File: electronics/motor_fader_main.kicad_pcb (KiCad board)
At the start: 2 copper layers, 59 x 17 mm, 30 parts, among them J1 Conn_01x04_MountingPin, J2 Program, J3 Conn_01x04_MountingPin, U1 ATtiny1616-M, U2 DRV8837

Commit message: Board cleanup, BOM cleanup
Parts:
- moved D2 0.75 mm to (75.2, 57.5)
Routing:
- net GND: track 8.58 -> 17.3 mm
- net VCC: track 95.3 -> 93.2 mm

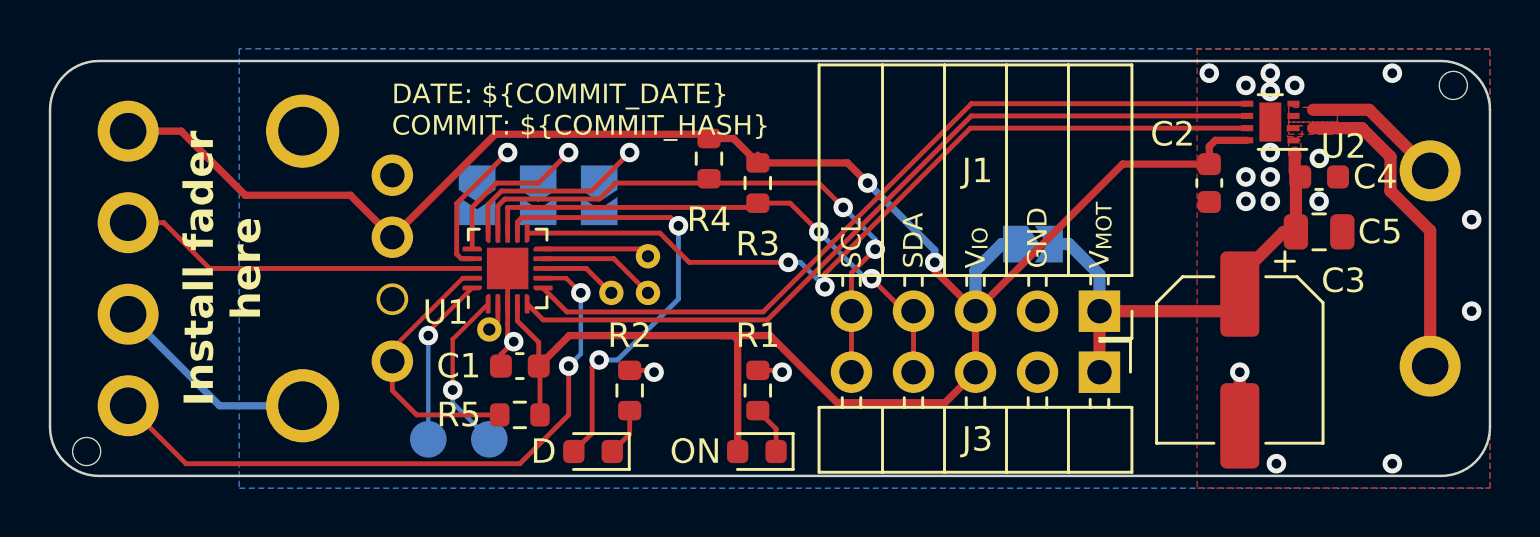
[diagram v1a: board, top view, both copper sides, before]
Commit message: Add JST SH I2C connectors
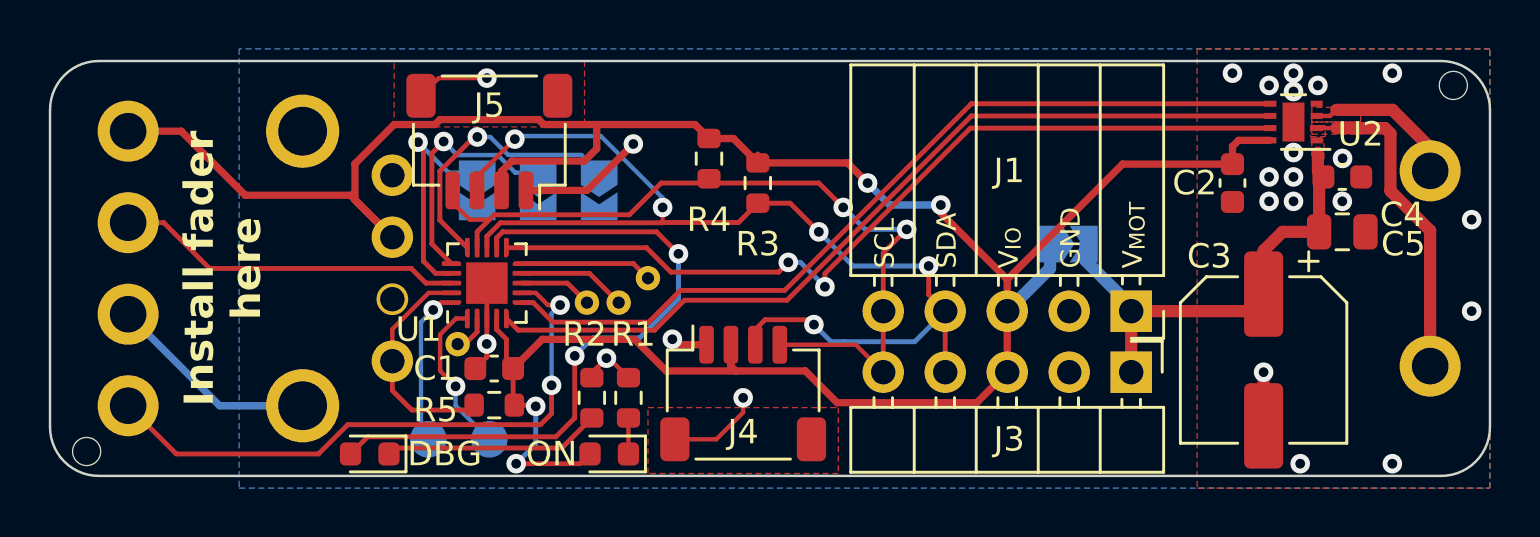
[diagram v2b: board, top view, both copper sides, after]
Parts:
- added J4: Conn_01x04_MountingPin, Connector_JST:JST_SH_SM04B-SRSS-TB_1x04-1MP_P1.00mm_Horizontal, F.Cu at (81.4, 55.1)
- added J5: Conn_01x04_MountingPin, Connector_JST:JST_SH_SM04B-SRSS-TB_1x04-1MP_P1.00mm_Horizontal, F.Cu at (71.0, 44.8)
- J1, J3: value Conn_01x04_MountingPin -> Conn_01x05
- moved D2 9.15 mm to (66.1, 57.6)
- moved D1 6.05 mm to (75.9, 57.6)
- moved R1 5.31 mm to (76.7, 55.3)
- moved R2 1.58 mm to (75.2, 55.3)
- moved TP6 1.43 mm to (69.7, 53.1)
- moved JP4 1.42 mm to (94.7, 49.0)
- moved J1 1.30 mm to (97.3, 51.8)
- moved J3 1.30 mm to (97.3, 54.2)
- moved TP5 1.26 mm to (76.3, 51.4)
- moved R5 1.12 mm to (71.2, 55.6)
- moved TP1 1.08 mm to (75.0, 51.4)
- moved C1 1.05 mm to (71.2, 54.1)
- moved U1 1.04 mm to (70.9, 50.6)
- moved C3 0.97 mm to (102.7, 53.8)
- moved C2 0.95 mm to (101.5, 46.5)
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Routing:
- net /SDA: track 22.1 -> 45.2 mm, vias 2 -> 5
- net VCC: track 93.2 -> 108.0 mm, vias 2 -> 4
- net GND: track 17.3 -> 30.4 mm, vias 21 -> 24
- net /SCL: track 23.8 -> 33.1 mm
- net /DBG_LED: track 18.7 -> 27.7 mm
- net Net-(D2-K): track 1.97 -> 8.92 mm
- net /M_1: track 33.2 -> 35.1 mm
- net /M_2: track 32.8 -> 34.7 mm
- net /M_SLEEP: track 33.4 -> 35.3 mm
- net /A0: track 7.42 -> 9.26 mm
- net /A2: track 9.53 -> 11.3 mm
- net /UPDI: track 11.0 -> 9.32 mm
- net /A1: track 8.26 -> 9.93 mm
- net /R_FADER: track 26.9 -> 25.2 mm
- net /MOTOR_B: track 12.9 -> 14.2 mm
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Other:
- board text added: "DBG"
- board text removed: "D"

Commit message: 3d model and update links in readme
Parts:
- J4, J5: footprint Connector_JST:JST_SH_SM04B-SRSS-TB_1x04-1MP_P1.00mm_Horizontal -> modified:JST_SH_SM04B-SRSS-TB_1x04-1MP_P1.00mm_Horizontal
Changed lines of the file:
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@@
 		)
 	)
-	(footprint "Connector_JST:JST_SH_SM04B-SRSS-TB_1x04-1MP_P1.00mm_Horizontal"
+	(footprint "modified:JST_SH_SM04B-SRSS-TB_1x04-1MP_P1.00mm_Horizontal"
 		(layer "F.Cu")
 		(at 81.4 55.125)
@@
 			)
 		)
-		(property "Footprint" "Connector_JST:JST_SH_SM04B-SRSS-TB_1x04-1MP_P1.00mm_Horizontal"
+		(property "Footprint" "modified:JST_SH_SM04B-SRSS-TB_1x04-1MP_P1.00mm_Horizontal"
 			(at 0 0 0)
 			(unlocked yes)
@@
 		)
 		(model "${KICAD8_3DMODEL_DIR}/Connector_JST.3dshapes/JST_SH_SM04B-SRSS-TB_1x04-1MP_P1.00mm_Horizontal.wrl"
+			(hide yes)
 			(offset
 				(xyz 0 0 0)
@@
 			(rotate
 				(xyz 0 0 0)
+			)
+		)
+		(model "${KIPRJMOD}/lib/misc.3dmodels/SM04B-SRSS-TB.STEP"
+			(offset
+				(xyz 0 1.3 -0.3)
+			)
+			(scale
+				(xyz 1 1 1)
+			)
+			(rotate
+				(xyz -90 0 0)
 			)
 		)
@@
 		)
 	)
-	(footprint "Connector_JST:JST_SH_SM04B-SRSS-TB_1x04-1MP_P1.00mm_Horizontal"
+	(footprint "modified:JST_SH_SM04B-SRSS-TB_1x04-1MP_P1.00mm_Horizontal"
 		(layer "F.Cu")
 		(at 71 44.8 180)
@@
 		(tags "connector JST SH horizontal")
 		(property "Reference" "J5"
-			(at 0 1.475 0)
+			(at 0 1.575 180)
 			(layer "F.SilkS")
 			(effects
@@
 		)
 		(property "Value" "Conn_01x04_MountingPin"
-			(at 0 3.98 0)
-			(layer "F.Fab")
-			(effects
-				(font
-					(size 1 1)
-					(thickness 0.15)
-				)
-			)
-		)
-		(property "Footprint" "Connector_JST:JST_SH_SM04B-SRSS-TB_1x04-1MP_P1.00mm_Horizontal"
+			(at 0 3.98 180)
+			(layer "F.Fab")
+			(effects
+				(font
+					(size 1 1)
+					(thickness 0.15)
+				)
+			)
+		)
+		(property "Footprint" "modified:JST_SH_SM04B-SRSS-TB_1x04-1MP_P1.00mm_Horizontal"
 			(at 0 0 180)
 			(unlocked yes)
@@
 		)
 		(fp_text user "${REFERENCE}"
-			(at 0 0 0)
+			(at 0 0 180)
 			(layer "F.Fab")
 			(effects
@@
 		)
 		(model "${KICAD8_3DMODEL_DIR}/Connector_JST.3dshapes/JST_SH_SM04B-SRSS-TB_1x04-1MP_P1.00mm_Horizontal.wrl"
+			(hide yes)
 			(offset
 				(xyz 0 0 0)
@@
 			)
 		)
+		(model "${KIPRJMOD}/lib/misc.3dmodels/SM04B-SRSS-TB.STEP"
+			(offset
+				(xyz 0 1.3 -0.3)
+			)
+			(scale
+				(xyz 1 1 1)
+			)
+			(rotate
+				(xyz -90 0 0)
+			)
+		)

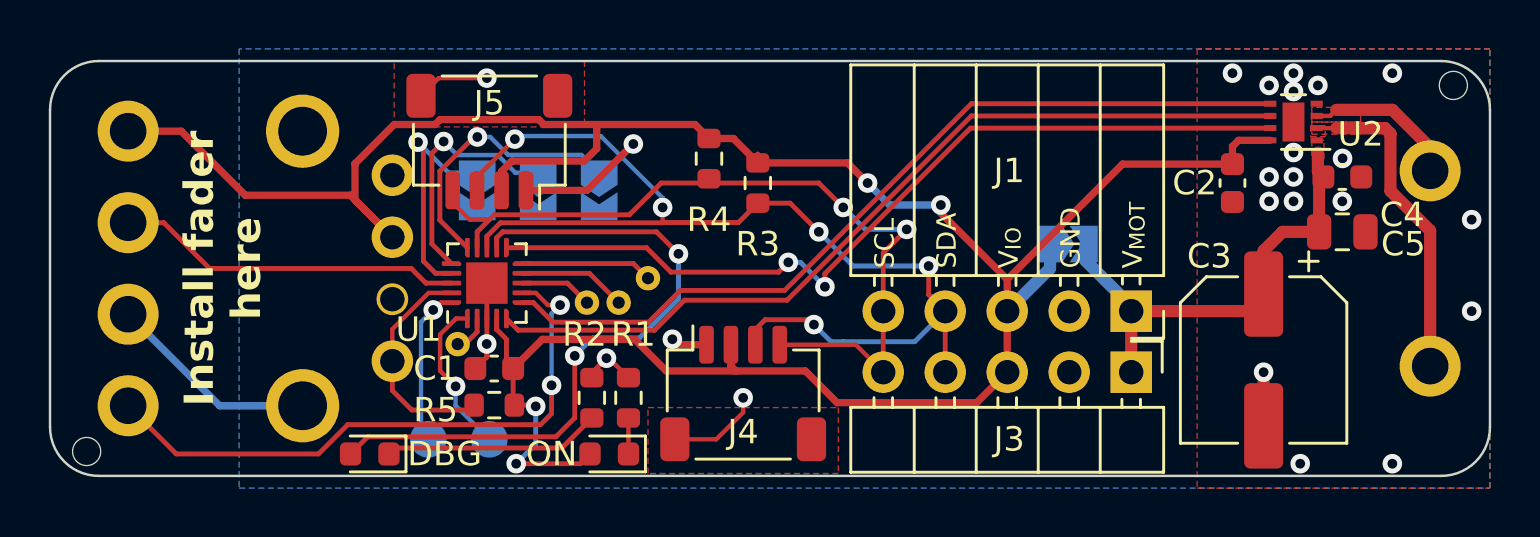
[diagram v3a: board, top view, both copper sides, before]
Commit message: Move UPDI header
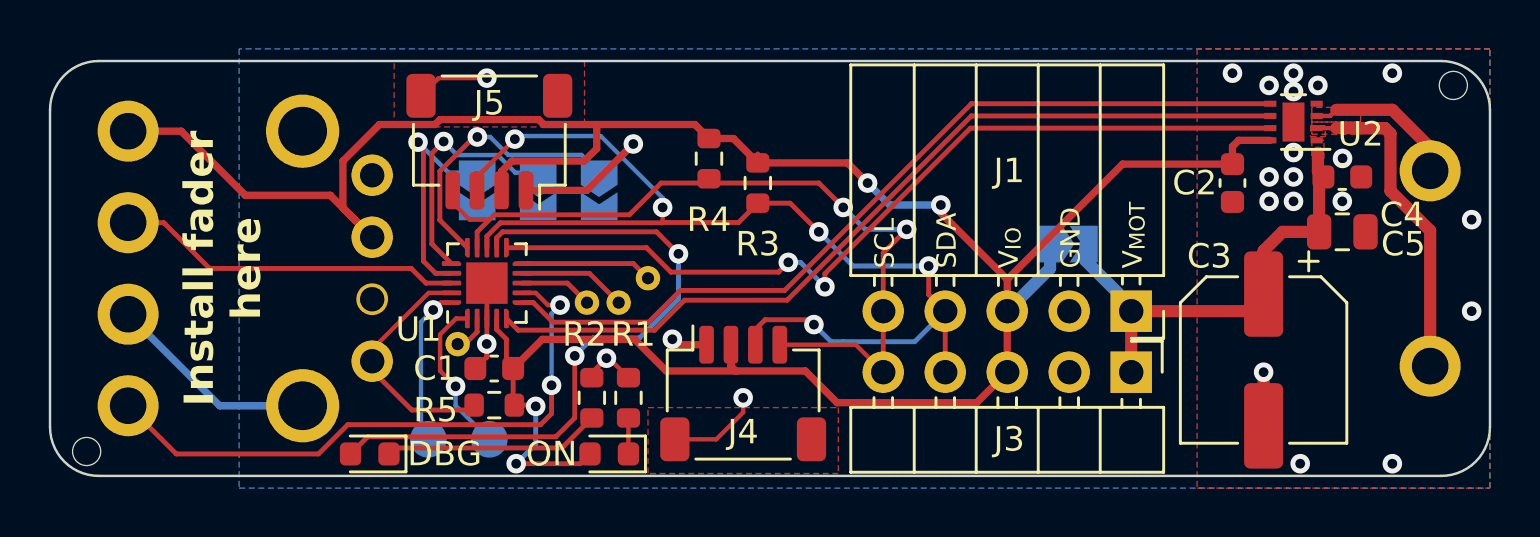
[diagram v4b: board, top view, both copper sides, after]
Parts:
- moved J2 0.83 mm to (66.2, 53.8)
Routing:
- net /UPDI: track 9.32 -> 10.0 mm
